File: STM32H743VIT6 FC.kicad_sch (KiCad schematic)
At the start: 35 parts, among them J2 DX07S016JA3R1500, SW2 SW_Push, U1 STM32H743VITx, U2 USBLC6-2SC6, U3 ICM-42688-P

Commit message: hjm
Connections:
- net NRST: no longer names the net of C_RESET1.1, U1.14 (NRST)
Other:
- note added: "Flash Memory CHECK!"
- note removed: "Flash Memory"
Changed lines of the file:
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@@
 		)
 	)
-	(text "Flash Memory\n"
+	(text "Flash Memory\nCHECK!"
 		(exclude_from_sim no)
 		(at 204.47 238.76 0)
@@
 	)
 	(junction
-		(at 46.99 80.01)
-		(diameter 0)
-		(color 0 0 0 0)
-	)
-	(junction
 		(at 106.68 78.74)
 		(diameter 0)
@@
 	(wire
 		(pts
-			(xy 41.91 80.01) (xy 46.99 80.01)
-		)
-		(stroke
-			(width 0)
-			(type default)
-		)
-	)
-	(wire
-		(pts
 			(xy 74.93 26.67) (xy 85.09 26.67)
 		)
@@
 		)
 	)
-	(global_label "NRST"
-		(shape input)
-		(at 41.91 80.01 180)
-		(fields_autoplaced yes)
-		(effects
-			(font
-				(size 1.27 1.27)
-			)
-			(justify right)
-		)
-		(property "Intersheetrefs" "${INTERSHEET_REFS}"
-			(at -8.255 -15.875 0)
-			(effects
-				(font
-					(size 1.27 1.27)
-				)
-				(hide yes)
-			)
-		)
-	)
 	(global_label "GYRO_MOSI"
 		(shape input)
@@
 				)
 				(justify left)
+				(hide yes)
 			)
 		)

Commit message: labels
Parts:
- removed C12, C14, C15, C16, C17, C3, C5, C_RESET1: 100n, Capacitor_SMD:C_0402_1005Metric, symbol Device:C_Small
- removed C19: 4u7, Capacitor_SMD:C_0603_1608Metric, symbol Device:C
- added FB1: FerriteBead, Inductor_SMD:L_0603_1608Metric, symbol Device:FerriteBead
- added H1, H2, H3, H4: MountingHole, MountingHole:MountingHole_4.3mm_M4, symbol Mechanical:MountingHole
- added MCU_C1, MCU_C9: 4u7, Capacitor_SMD:C_0603_1608Metric, symbol Device:C
- added MCU_C10, MCU_C12, MCU_C2, MCU_C3, MCU_C4, MCU_C5, MCU_C6, MCU_C7, MCU_C8: 100n, Capacitor_SMD:C_0402_1005Metric, symbol Device:C
- added MCU_C11: 4u7, Capacitor_SMD:C_0402_1005Metric, symbol Device:C
- IMU_C1: renamed from C4; value 0.1u -> 0u1
- USB_C1: renamed from C13; value 100nF -> 100n
- U_STM32: renamed from U1; value STM32H743VITx -> STM32H743VIT6
- renumbered C_dps1 to BARO_C1, C_dps2 to BARO_C2, C_flash1 to FLASH_C1, R_flash1 to FLASH_R1, R_flash2 to FLASH_R2, C7 to IMU_C2, C10 to IMU_C3, J2 to J_USB, C_vcap1 to MCU_C13, C_vcap2 to MCU_C14, R1 to MCU_R1, R4 to USB_R1, R5 to USB_R2, R18 to USB_R3, R17 to USB_R4, U_BARO1 to U_BARO, U_flash1 to U_FLASH, U3 to U_IMU
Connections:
- net 3V3_IMU is gone; now on net 3.3V: BARO_C1.2, BARO_C2.2, U_BARO.6 (VDDIO), U_BARO.8 (VDD)
- net 3V3_MCU_OSD is gone; now on net 3.3V: FLASH_C1.1, FLASH_R1.1, FLASH_R2.1, U_FLASH.8 (VCC)
- net GND: now also USB_C1.1, USB_R2.1, MCU_C1.2, MCU_C10.2, MCU_C11.2, MCU_C12.2, MCU_C2.2, MCU_C3.2, MCU_C4.2, MCU_C5.2, MCU_C6.2, MCU_C7.2, MCU_C8.2, MCU_C9.2; no longer USB_C1.2, USB_R2.2
- net at U_STM32.14 (NRST): now also MCU_C10.1
- net 3.3VA: now reaches U_STM32.20 (VREF+)
- net 3.3VA: now also U_STM32.21 (VDDA), FB1.1, MCU_C11.1, MCU_C12.1, MCU_C8.1, MCU_C9.1
- net at J_USB.B5 (CC2): now also USB_R2.2; no longer USB_R2.1
- net +3V3 renamed 3.3V
- net 3.3V: now also FB1.2, MCU_C1.1, MCU_C2.1, MCU_C3.1, MCU_C4.1, MCU_C5.1, MCU_C6.1, MCU_C7.1; no longer U_STM32.21 (VDDA)
- net +5V_USB renamed 5V_USB
- net 5V_USB: now also USB_C1.2; no longer USB_C1.1
- net SPI3_MISO_PIN  renamed SPI3_MISO_PIN
- net vcap1: no longer names the net of MCU_C13.1, U_STM32.48 (VCAP)
- net vcap2: no longer names the net of MCU_C14.1, U_STM32.73 (VCAP)
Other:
- note added: "BOOT"
- note added: "Decoupling"
- note added: "Mounting Holes"
- note added: "VREF"
- note removed: "ESD Protection"
- moved on the sheet: 3.3_R1, BARO_C1, D1, IMU_C1, IMU_C3, J_USB, MCU_C13, MCU_C14, MCU_R1, SW2, U2, USB_C1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

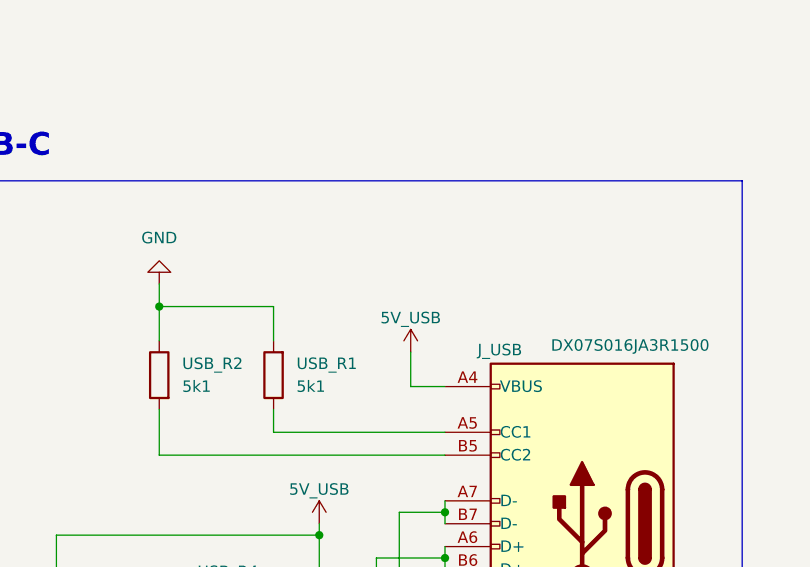
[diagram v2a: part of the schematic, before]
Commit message: power mux
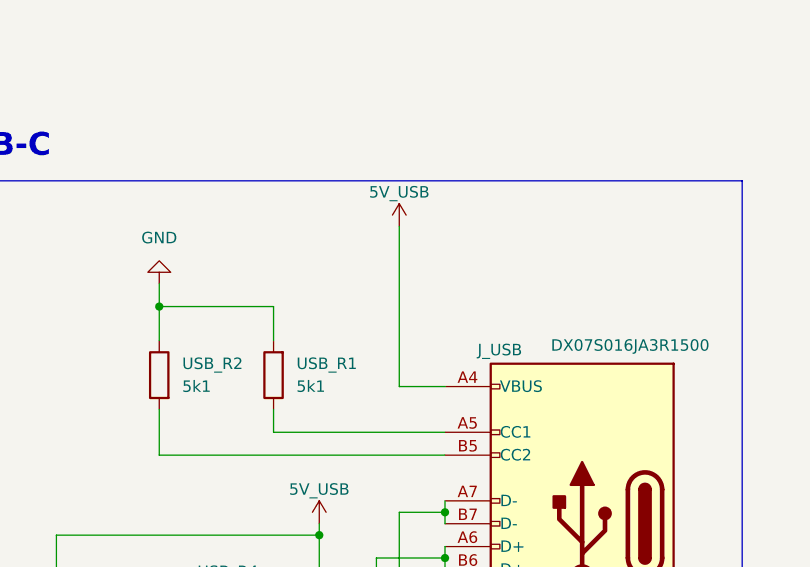
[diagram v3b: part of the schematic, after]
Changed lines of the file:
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@@
 	(wire
 		(pts
-			(xy 228.6 107.95) (xy 228.6 111.76)
+			(xy 227.33 93.98) (xy 227.33 111.76)
 		)
 		(stroke
@@
 	(wire
 		(pts
-			(xy 232.41 111.76) (xy 228.6 111.76)
+			(xy 232.41 111.76) (xy 227.33 111.76)
 		)
 		(stroke
@@
 	(symbol
 		(lib_id "power:+3.3V")
-		(at 228.6 107.95 0)
+		(at 227.33 93.98 0)
 		(unit 1)
 		(exclude_from_sim no)
@@
 		(dnp no)
 		(property "Reference" "#PWR037"
-			(at 228.6 111.76 0)
+			(at 227.33 97.79 0)
 			(effects
 				(font
@@
 		)
 		(property "Value" "5V_USB"
-			(at 228.6 104.14 0)
+			(at 227.33 90.17 0)
 			(effects
 				(font
@@
 		)
 		(property "Footprint" ""
-			(at 228.6 107.95 0)
+			(at 227.33 93.98 0)
 			(effects
 				(font
@@
 		)
 		(property "Datasheet" ""
-			(at 228.6 107.95 0)
+			(at 227.33 93.98 0)
 			(effects
 				(font
@@
 		)
 		(property "Description" "Power symbol creates a global label with name \"+3.3V\""
-			(at 228.6 107.95 0)
+			(at 227.33 93.98 0)
 			(effects
 				(font

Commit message: single sheet
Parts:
- added 3V3_0, 5V_R0, 9V_R0, USB_R0: 1k5, Resistor_SMD:R_0402_1005Metric, symbol Device:R
- added 3V3_C4, 3v3_C3: 4u7, Capacitor_SMD:C_0805_2012Metric, symbol Device:C_Small
- added 3V3_D, 5V_D, 9V_D, USB_D: RED, LED_SMD:LED_0603_1608Metric, symbol Device:LED
- added 5V_C10, 5V_C11, 9V_C10, 9V_C11: 22u, Capacitor_SMD:C_0805_2012Metric, symbol Device:C
- added 5V_C12, 9V_C12: 75p, Capacitor_SMD:C_0402_1005Metric, symbol Device:C
- added 5V_C7, 9V_C7: 10u, Capacitor_SMD:C_0603_1608Metric, symbol Device:C
- added 5V_C8, 5V_C9, 9V_C8, 9V_C9: 0u1, Capacitor_SMD:C_0402_1005Metric, symbol Device:C
- added 5V_L2: 10u, Capacitor_SMD:C_0603_1608Metric, symbol Device:L
- added 5V_R5, 9V_R5: 511k, Resistor_SMD:R_0603_1608Metric, symbol Device:R
- added 5V_R6, 9V_R6: 105k, Resistor_SMD:R_0603_1608Metric, symbol Device:R
- added 5V_R7, 9V_R7: 100k, Resistor_SMD:R_0603_1608Metric, symbol Device:R
- added 5V_R8: 13.3k, Resistor_SMD:R_0402_1005Metric, symbol Device:R
- added 9V_L2: 15u, Capacitor_SMD:C_0603_1608Metric, symbol Device:L
- added 9V_R8: 7k, Resistor_SMD:R_0402_1005Metric, symbol Device:R
- added D_5V1, D_5V_USB1: B340A-13-F, custom_Library:Schottky BA340 SMA_L4.4-W2.6-LS5.0-RD, symbol custom_Library:B340A-13-F
- added MUX_C2: 100n, Capacitor_SMD:C_0603_1608Metric, symbol Device:C_Small
- added MUX_R10: 60, Resistor_SMD:R_0603_1608Metric, symbol Device:R_Small
- added MUX_R6: 13k, Resistor_SMD:R_0603_1608Metric, symbol Device:R_Small
- added MUX_R7, MUX_R9: 5k, Resistor_SMD:R_0603_1608Metric, symbol Device:R_Small
- added MUX_R8: 43k, Resistor_SMD:R_0603_1608Metric, symbol Device:R_Small
- added U1, U3: TPS54302DDCR, Package_TO_SOT_SMD:SOT-23-6, symbol Regulator_Switching:TPS54302
- added U3_MUX1: TPS2121RUXR, TPS2121RUXR:RUX0012A, symbol ul_TPS2121RUXR:TPS2121RUXR
- added U_3V1: LP5912-3.3DRVR, custom_Library:LP59123.3_SON65P200X200X80-7N, symbol custom_Library:LP5912-3.3DRVR
- renumbered 3.3_R1 to 3.3V_R0, D1 to MCU_D
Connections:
- net 3.3V: now also MCU_D.2 (A), 3V3_C4.1, 3V3_D.2 (A), U_3V1.1 (OUT)
- net 5V_USB: now also D_5V_USB1.2 (A), MUX_R6.2, U3_MUX1.7 (IN1), USB_D.2 (A)
- net GND: now also 3.3V_R0.2, 3V3_0.2, 3V3_C4.2, 3v3_C3.1, 5V_C10.2, 5V_C11.2, 5V_C7.2, 5V_C8.2, 5V_R0.2, 5V_R6.2, 5V_R8.2, 9V_C10.2, 9V_C11.2, 9V_C7.2, 9V_C8.2, 9V_R0.2, 9V_R6.2, 9V_R8.2, MUX_C2.1, MUX_R10.2, MUX_R7.1, MUX_R9.1, U1.1 (GND), U3.1 (GND), U3_MUX1.12 (GND), U3_MUX1.4 (OV2), U3_MUX1.5 (OV1), U3_MUX1.9 (ST), USB_R0.2, U_3V1.5 (GND), U_3V1.7 (EXP)
- new net: 9V_R5.2, 9V_R6.1, U3.5 (EN)
- new net: 5V_D.1 (K), 5V_R0.1
- new net: 5V_C12.2, 5V_R7.2, 5V_R8.1, U1.4 (FB)
- new net: MUX_R8.1, MUX_R9.2, U3_MUX1.3 (CP2)
- new net: 5V_C9.1, U1.6 (BOOT)
- new net: 5V_C9.2, 5V_L2.1, U1.2 (SW)
- new net: MUX_R6.1, MUX_R7.2, U3_MUX1.6 (PR1)
- new net: MUX_R10.1, U3_MUX1.10 (ILM)
- new net: MUX_C2.2, U3_MUX1.11 (SS)
- new net: 3V3_0.1, 3V3_D.1 (K)
- new net: 5V_R5.2, 5V_R6.1, U1.5 (EN)
- new net: 9V_C12.2, 9V_R7.2, 9V_R8.1, U3.4 (FB)
- new net: 9V_D.1 (K), 9V_R0.1
- new net: USB_D.1 (K), USB_R0.1
- new net: 9V_C9.2, 9V_L2.1, U3.2 (SW)
- new net: 9V_C9.1, U3.6 (BOOT)
- new net 5V: 3v3_C3.2, U3_MUX1.1 (OUT), U3_MUX1.8 (OUT), U_3V1.4 (EN), U_3V1.6 (IN)
- new net 5V_BEC: D_5V1.2 (A)
- new net 5V_BUS: D_5V1.1 (K), D_5V_USB1.1 (K)
- new net 5V_REG: 5V_C10.1, 5V_C11.1, 5V_C12.1, 5V_D.2 (A), 5V_L2.2, 5V_R7.1, MUX_R8.2, U3_MUX1.2 (IN2)
- new net 9V_REG: 9V_C10.1, 9V_C11.1, 9V_C12.1, 9V_D.2 (A), 9V_L2.2, 9V_R7.1
- new net LIPO: 5V_C7.1, 5V_C8.1, 5V_R5.1, 9V_C7.1, 9V_C8.1, 9V_R5.1, U1.3 (VIN), U3.3 (VIN)
- no-connect marks 8 -> 9
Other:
- note added: "5V -> 3V3 @500mA"
- note added: "BAT -> 5V @3A"
- note added: "BAT -> 9V @3A"
- note added: "Diodes: 40V/3A 500mV 850mW"
- note added: "LEDS"
- note added: "Power Mux"
- note added: "Power Path"
- note removed: "leds"
- moved on the sheet: 3.3V_R0, MCU_D

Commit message: labels
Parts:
- 5V_R0, USB_R0: value 1k5 -> 3k6
- 9V_R0: value 1k5 -> 8k2
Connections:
- net 3.3V: no longer MCU_D.2 (A)
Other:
- removed sheet power
- note added: "Barometer"
- note removed: "Baro"
- moved on the sheet: 3V3_C4, 3v3_C3, MCU_R1, SW2, U_3V1

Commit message: res
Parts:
- 5V_R8: value 13.3k -> 13k3
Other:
- moved on the sheet: H1, H2, H3, H4
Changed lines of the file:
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@@
 	)
 	(rectangle
-		(start 381 19.05)
-		(end 402.59 54.61)
+		(start 403.86 43.18)
+		(end 425.45 78.74)
 		(stroke
 			(width 0)
@@
 	(text "Mounting Holes"
 		(exclude_from_sim no)
-		(at 388.366 17.526 0)
+		(at 411.226 41.656 0)
 		(effects
 			(font
@@
 	(symbol
 		(lib_id "Mechanical:MountingHole")
-		(at 384.81 22.86 0)
+		(at 407.67 46.99 0)
 		(unit 1)
 		(exclude_from_sim yes)
@@
 		(fields_autoplaced yes)
 		(property "Reference" "H1"
-			(at 387.35 21.5899 0)
+			(at 410.21 45.7199 0)
 			(effects
 				(font
@@
 		)
 		(property "Value" "MountingHole"
-			(at 387.35 24.1299 0)
+			(at 410.21 48.2599 0)
 			(effects
 				(font
@@
 		)
 		(property "Footprint" "MountingHole:MountingHole_4.3mm_M4"
-			(at 384.81 22.86 0)
+			(at 407.67 46.99 0)
 			(effects
 				(font
@@
 		)
 		(property "Datasheet" "~"
-			(at 384.81 22.86 0)
+			(at 407.67 46.99 0)
 			(effects
 				(font
@@
 		)
 		(property "Description" "Mounting Hole without connection"
-			(at 384.81 22.86 0)
+			(at 407.67 46.99 0)
 			(effects
 				(font
@@
 	(symbol
 		(lib_id "Mechanical:MountingHole")
-		(at 384.81 49.53 0)
+		(at 407.67 73.66 0)
 		(unit 1)
 		(exclude_from_sim yes)
@@
 		(fields_autoplaced yes)
 		(property "Reference" "H4"
-			(at 387.35 48.2599 0)
+			(at 410.21 72.3899 0)
 			(effects
 				(font
@@
 		)
 		(property "Value" "MountingHole"
-			(at 387.35 50.7999 0)
+			(at 410.21 74.9299 0)
 			(effects
 				(font
@@
 		)
 		(property "Footprint" "MountingHole:MountingHole_4.3mm_M4"
-			(at 384.81 49.53 0)
+			(at 407.67 73.66 0)
 			(effects
 				(font
@@
 		)
 		(property "Datasheet" "~"
-			(at 384.81 49.53 0)
+			(at 407.67 73.66 0)
 			(effects
 				(font
@@
 		)
 		(property "Description" "Mounting Hole without connection"
-			(at 384.81 49.53 0)
+			(at 407.67 73.66 0)
 			(effects
 				(font
@@
 	(symbol
 		(lib_id "Mechanical:MountingHole")
-		(at 384.81 31.75 0)
+		(at 407.67 55.88 0)
 		(unit 1)
 		(exclude_from_sim yes)
@@
 		(fields_autoplaced yes)
 		(property "Reference" "H2"
-			(at 387.35 30.4799 0)
+			(at 410.21 54.6099 0)
 			(effects
 				(font
@@
 		)
 		(property "Value" "MountingHole"
-			(at 387.35 33.0199 0)
+			(at 410.21 57.1499 0)
 			(effects
 				(font
@@
 		)
 		(property "Footprint" "MountingHole:MountingHole_4.3mm_M4"
-			(at 384.81 31.75 0)
+			(at 407.67 55.88 0)
 			(effects
 				(font
@@
 		)
 		(property "Datasheet" "~"
-			(at 384.81 31.75 0)
+			(at 407.67 55.88 0)
 			(effects
 				(font
@@
 		)
 		(property "Description" "Mounting Hole without connection"
-			(at 384.81 31.75 0)
+			(at 407.67 55.88 0)
 			(effects
 				(font
@@
 	(symbol
 		(lib_id "Mechanical:MountingHole")
-		(at 384.81 40.64 0)
+		(at 407.67 64.77 0)
 		(unit 1)
 		(exclude_from_sim yes)
@@
 		(fields_autoplaced yes)
 		(property "Reference" "H3"
-			(at 387.35 39.3699 0)
+			(at 410.21 63.4999 0)
 			(effects
 				(font
@@
 		)
 		(property "Value" "MountingHole"
-			(at 387.35 41.9099 0)
+			(at 410.21 66.0399 0)
 			(effects
 				(font
@@
 		)
 		(property "Footprint" "MountingHole:MountingHole_4.3mm_M4"
-			(at 384.81 40.64 0)
+			(at 407.67 64.77 0)
 			(effects
 				(font
@@
 		)
 		(property "Datasheet" "~"
-			(at 384.81 40.64 0)
+			(at 407.67 64.77 0)
 			(effects
 				(font
@@
 		)
 		(property "Description" "Mounting Hole without connection"
-			(at 384.81 40.64 0)
+			(at 407.67 64.77 0)
 			(effects
 				(font
@@
 			)
 		)
-		(property "Value" "13.3k"
+		(property "Value" "13k3"
 			(at 580.39 351.79 0)
 			(effects

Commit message: bat
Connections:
- net LIPO: no longer 5V_C7.1, 5V_C8.1, 5V_R5.1, 9V_C7.1, 9V_C8.1, 9V_R5.1, U1.3 (VIN), U3.3 (VIN)
- new net BAT: 5V_C7.1, 5V_C8.1, 5V_R5.1, 9V_C7.1, 9V_C8.1, 9V_R5.1, U1.3 (VIN), U3.3 (VIN)
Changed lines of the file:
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@@
 			)
 		)
-		(property "Value" "LIPO"
+		(property "Value" "BAT"
 			(at 468.122 310.642 0)
 			(effects
@@
 			)
 		)
-		(property "Value" "LIPO"
+		(property "Value" "BAT"
 			(at 468.122 385.572 0)
 			(effects

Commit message: schottky
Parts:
- added D0: BAT54C, Package_TO_SOT_SMD:SOT-23, symbol Diode:BAT54C
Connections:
- net 5V: now also D0.3
- net 5V_REG: now also D0.2
- net 5V_USB: now also D0.1
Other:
- note added: "Schottky Diode"
